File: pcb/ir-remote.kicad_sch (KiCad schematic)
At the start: 109 parts, among them J1 Jack_RCA_Stereo, J12 Conn_01x04, J2 Jack_RCA_Stereo, J3 Conn_02x04, J4 USB-C_Receptacle_Molex_217179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, U1 STM32G431CBTx, U10 LMR62421XMF, U2 TSOP38238, U3 NE5532, U4 NE5532, U5 LP5024RSMR, U6 USBLC6-2SC6, U7 DRV8210DRLR, U9 PCM3060PW, X10 16MHz_18pF_FA238

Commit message: PCB WIP
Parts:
- removed C129, C132, C138: 10uF_0805_25V, 4ms_Capacitor:C_0805, symbol 4ms_Capacitor:10uF_0805_25V
- removed C18: 100nF_0603_16V, 4ms_Capacitor:C_0603, symbol 4ms_Capacitor:100nF_0603_16V
- removed C32: 2.2uF_0603_25V, 4ms_Capacitor:C_0603, symbol 4ms_Capacitor:2.2uF_0603_25V
- removed C6: 1nF_0603_50V, 4ms_Capacitor:C_0603, symbol 4ms_Capacitor:1nF_0603_50V
- removed D1: D_SOD-323F_DNP, 4ms_Diode:D_SOD-123F, symbol 4ms_Diode:D_SOD-323F_DNP
- removed L1: 2.2uH_2.4A_2016, Inductor_SMD:L_Taiyo-Yuden_NR-20xx_HandSoldering, symbol 4ms_Inductor:2.2uH_2.4A_2016
- removed LED1, LED2, LED3, LED4, LED5, LED6, LED7, LED8: RGB_CA_RightAngle, 4ms_LED:LED_Kingbright_APFA2507LQBDSEEZGKC_2.5x1.0mm_Horizontal_RGB, symbol 4ms_LED:RGB_CA_RightAngle
- removed R13, R2, R4: 10k_0603, 4ms_Resistor:R_0603, symbol 4ms_Resistor_0603:10k_0603
- removed R21: 4.99k_0603, 4ms_Resistor:R_0603, symbol 4ms_Resistor_0603:4.99k_0603
- removed R3: 42.2k_0603, 4ms_Resistor:R_0603, symbol 4ms_Resistor_0603:42.2k_0603
- removed U10: LMR62421XMF, Package_TO_SOT_SMD:SOT-23-5, symbol 4ms_IC:LMR62421XMF
- removed U5: LP5024RSMR, 4ms_Package_QFP:QFN-32-1EP_4x4mm_P0.4mm_EP2.65x2.65mm, symbol 4ms_IC:LP5024RSMR
- added C300: 1uF_0402_25V, 4ms_Capacitor:C_0402, symbol 4ms_Capacitor:1uF_0402_25V
- added C303, C6: 10uF_0805_25V, 4ms_Capacitor:C_0805, symbol 4ms_Capacitor:10uF_0805_25V
- added L3: 10uH_0805_0.5A, 4ms_Resistor:R_0805_2012Metric, symbol 4ms_Inductor:10uH_0805_0.5A
- added R4: 71.5k_0603, 4ms_Resistor:R_0603, symbol 4ms_Resistor_0603:71.5k_0603
- added R5: 10k_0603, 4ms_Resistor:R_0603, symbol 4ms_Resistor_0603:10k_0603
- added U112: TLV61046ADB, Package_TO_SOT_SMD:SOT-23-6, symbol Regulator_Switching:TLV61046ADB
- J1, J2: footprint (none) -> 4ms_Jack:RCA_Stereo_SwitchCraft-PJRAS2X1S
- POT1: footprint 4ms_Potentiometer: -> 4ms_Potentiometer:Slider_Dual_Motorized_PSM60-081A-xxx
- U7: JLCPCB ID (none) -> C3681297
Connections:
- net +5VA: now also C100.2, C102.2, D101.2 (cathode), D102.2 (cathode), U3.8 (V+), U4.8 (V+)
- net GND: now also C300.2, C303.2, C6.2, R5.2, U112.2 (GND)
- net I2C_SCL: now also U1.39 (PA15); no longer U1.31 (PA9)
- net I2C_SDA: now also U1.44 (PB7); no longer U1.30 (PA8)
- net MOT+: now also U1.31 (PA9)
- net MOT-: now also U1.30 (PA8)
- net VDD: now also U7.5 (VM), C303.1, C6.1, R4.1, U112.5 (VOUT); no longer C100.2, C102.2, D101.2 (cathode), D102.2 (cathode), U3.8 (V+), U4.8 (V+)
- net V_USB: now also C300.1, L3.1, U112.4 (EN), U112.6 (VI); no longer U7.5 (VM)
- net at POT1.MOTORA: now also U7.6 (OUT1); no longer U7.4 (OUT2)
- net at POT1.MOTORB: now also U7.4 (OUT2); no longer U7.6 (OUT1)
- net USB_DP: now reaches J4.A6 (D+1), J4.B6 (D+2), U6.3 (I/O2), U6.4 (I/O2)
- net USB_DP: now also U1.34 (PA12)
- net USB_DM: now reaches J4.A7 (D-1), J4.B7 (D-2), U6.1 (I/O1), U6.6 (I/O1)
- net USB_DM: now also U1.33 (PA11)
- new net: R4.2, R5.1, U112.3 (FB)
- new net: L3.2, U112.1 (SW)
- no-connect marks 31 -> 25
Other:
- note added: "6.5V Supply"
- note added: "Digital supply"
- note added: "R4/R5 = (VOUt/0.795V - 1)"
- note removed: "LED Driver"
- note removed: "VDD 6.5V"
- moved on the sheet: C31, C4, C40, C49, C5, C51, NT1, NT11, POT1A, POT1B, POT1C, POT1D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

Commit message: PCB WIP
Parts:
- removed C100, C102, C41, C42, C45: 100nF_0402_16V, 4ms_Capacitor:C_0402, symbol 4ms_Capacitor:100nF_0402_16V
- removed C104, C105, C125, C126: 1uF_0402_25V, 4ms_Capacitor:C_0402, symbol 4ms_Capacitor:1uF_0402_25V
- removed C115, C116: 1.5nF_0402_50V, 4ms_Capacitor:C_0402, symbol 4ms_Capacitor:1.5nF_0402_50V
- removed C121, C122, C123, C124: 560pF_0402_50v, 4ms_Capacitor:C_0402, symbol 4ms_Capacitor:560pF_0402_50v
- removed C44: 22uF_0805_25V, 4ms_Capacitor:C_0805, symbol 4ms_Capacitor:22uF_0805_25V
- removed C49: 2.2uF_0603_25V, 4ms_Capacitor:C_0603, symbol 4ms_Capacitor:2.2uF_0603_25V
- removed C51: 10uF_0603_10V, 4ms_Capacitor:C_0603, symbol 4ms_Capacitor:10uF_0603_10V
- removed D101, D102: BAT54S, 4ms_Package_SOT:SOT23-3_PO132, symbol 4ms_Diode:BAT54S
- removed J1, J2: Jack_RCA_Stereo, 4ms_Jack:RCA_Stereo_SwitchCraft-PJRAS2X1S, symbol 4ms_Connector:Jack_RCA_Stereo
- removed NT1: NetTie_2, NetTie:NetTie-2_SMD_Pad0.5mm, symbol Device:NetTie_2
- removed R105, R109, R110, R112, R113, R114, R124, R125: 100k_0402, 4ms_Resistor:R_0402, symbol 4ms_Resistor_0402:100k_0402
- removed R115, R126: 1k_0402, 4ms_Resistor:R_0402, symbol 4ms_Resistor_0402:1k_0402
- removed R119, R120, R121, R122: 10k_0603, 4ms_Resistor:R_0603, symbol 4ms_Resistor_0603:10k_0603
- removed R128, R131, R132, R135: 7.5k_0402, 4ms_Resistor:R_0402, symbol 4ms_Resistor_0402:7.5k_0402
- removed R129, R130, R133, R134: 820Ω_0402, 4ms_Resistor:R_0402, symbol 4ms_Resistor_0402:820Ω_0402
- removed R139, R140: 100Ω_0603, 4ms_Resistor:R_0603, symbol 4ms_Resistor_0603:100Ω_0603
- removed R141, R142: 47k_0603, 4ms_Resistor:R_0603, symbol 4ms_Resistor_0603:47k_0603
- removed R47, R48: 4.7k_0402, 4ms_Resistor:R_0402, symbol 4ms_Resistor_0402:4.7k_0402
- removed U3, U4: NE5532, Package_SO:SOIC-8_5.3x5.3mm_P1.27mm, symbol Amplifier_Operational:NE5532
- removed U9: PCM3060PW, Package_SO:TSSOP-28_4.4x9.7mm_P0.65mm, symbol 4ms_IC:PCM3060PW
- removed V1: AP2120N-5.0TRG1, 4ms_Package_SOT:SOT23-3_PO132, symbol 4ms_Regulator:AP2120N-5.0TRG1
- added C10, C11, C13, C15, C27, C28, C29, C30: 10uF_0603_10V, 4ms_Capacitor:C_0603, symbol 4ms_Capacitor:10uF_0603_10V
- added C12, C14, C33, C9: 0.1uF_0603_16V, 4ms_Capacitor:C_0603, symbol 4ms_Capacitor:0.1uF_0603_16V
- added C16, C19, C20, C21, C26, C32: 1uF_0603_25V, 4ms_Capacitor:C_0603, symbol 4ms_Capacitor:1uF_0603_25V
- added C17, C18: 22uF_1206_25V, 4ms_Capacitor:C_1206, symbol 4ms_Capacitor:22uF_1206_25V
- added C22, C23: 47nF_0603_35V, 4ms_Capacitor:C_0603, symbol 4ms_Capacitor:47nF_0603_35V
- added C7, C8: 47pF_0603_50V, 4ms_Capacitor:C_0603, symbol 4ms_Capacitor:47pF_0603_50V
- added J1, J2, J8: Conn_01x02, 4ms_Connector:Pins_1x02_2.54mm_TH, symbol 4ms_Connector:Conn_01x02
- added J5, J7: Jack_RCA_Stereo, 4ms_Jack:RCA_Stereo_SwitchCraft-PJRAS2X1S, symbol 4ms_Connector:Jack_RCA_Stereo
- added J6: Conn_01x03, 4ms_Connector:Pins_1x03_2.54mm_TH, symbol 4ms_Connector:Conn_01x03
- added JP1: SolderJumper_2_Open, 4ms_SolderJumper:JUMPER_SMD_1x2, symbol 4ms_Net_Tie:SolderJumper_2_Open
- added NT2: NetTie, 4ms_SolderJumper:NetTie-2_SMD_Pad0.16mm_6mil, symbol 4ms_Net_Tie:NetTie
- added R10, R11: 1k_0603, 4ms_Resistor:R_0603, symbol 4ms_Resistor_0603:1k_0603
- added R12, R9: 4.7k_0603, 4ms_Resistor:R_0603, symbol 4ms_Resistor_0603:4.7k_0603
- added R13, R16: 100Ω_0603, 4ms_Resistor:R_0603, symbol 4ms_Resistor_0603:100Ω_0603
- added R14, R15: 100k_0603, 4ms_Resistor:R_0603, symbol 4ms_Resistor_0603:100k_0603
- added R2, R3, R6, R7, R8: 27Ω_0603, 4ms_Resistor:R_0603, symbol 4ms_Resistor_0603:27Ω_0603
- added TP1, TP11, TP12, TP13, TP14, TP2, TP3, TP4, TP5, TP6, TP7, TP8: TestPoint, 4ms_TestPoint:TestPoint_WireHole, symbol 4ms_Connector:TestPoint
- added U3, U4: TLV74018, 4ms_Package_SOT:SOT-23-5, symbol 4ms_Regulator:TLV74018PDBV
- added U5: TLV320AIC3204, Package_DFN_QFN:QFN-32-1EP_5x5mm_P0.5mm_EP3.45x3.45mm_ThermalVias, symbol 4ms_IC:TLV320AIC3204
- added U8: TAR5S33U, 4ms_Package_SOT:SOT-563-5, symbol 4ms_Regulator:TAR5S33U
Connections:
- net +3V3: now also C11.1, C33.1, R9.1, U5.6 (IOVDD)
- net CODEC_RESET: now also U1.45 (PB8), U5.31 (RESET_N)
- net GND: now also C10.2, C11.2, C14.1, C27.2, C28.2, C29.2, C30.2, C32.2, C33.2, J8.1 (Pin_1), JP1.1 (A), NT2.1, R12.1, U3.2 (GND), U4.2 (GND), U5.28 (DVSS), U5.33 (PAD), U5.7 (IOVSS), U8.2 (GND); no longer U7.9 (GND)
- net GNDA: now also C12.1, C13.2, C15.2, C16.2, C22.2, C23.2, C7.2, C8.2, C9.1, J5.S1, J5.S2, J6.2 (Pin_2), J7.S1, J7.S2, NT2.2, R14.2, R15.2, U5.17 (AVSS)
- net I2C_SCL: now also U5.9 (SCL_SS_N)
- net I2C_SDA: now also U5.10 (SDA_MOSI)
- net SAI_FS: now also R8.1
- net SAI_MCLK: now also R6.1
- net SAI_SCK: now also R7.1
- net SAI_SD_A: now also R2.1
- net SAI_SD_B: now also R3.1
- net V_USB: now also C40.1, V12.1 (VI), C28.1, C29.1, C32.1, U3.1 (IN), U3.3 (EN), U4.1 (IN), U4.3 (EN), U8.1 (EN), U8.5 (IN)
- net at J4.SH1 (Shield1), J4.SH2 (Shield2), J4.SH3 (Shield3)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: now also J8.2 (Pin_2)
- net VDD renamed Vmotor
- net Vmotor: no longer C40.1, V12.1 (VI)
- new net: R7.2, U5.2 (BCLK)
- new net: C14.2, U8.3 (Noise)
- new net: C19.1, R10.2
- new net: R8.2, U5.3 (WCLK)
- new net: C13.1, J1.1 (Pin_1), U5.24 (AVDD)
- new net: C19.2, J5.T2, R14.1
- new net: C23.1, J7.T2, R16.2
- new net: JP1.2 (B), R9.2, U5.30 (LDO_SELECT)
- new net: C20.1, R11.2
- new net: C21.2, R13.1
- new net: C22.1, J7.T1, R13.2
- new net: C18.1, U5.27 (HPR)
- new net: C18.2, J6.3 (Pin_3)
- new net: C26.2, R16.1
- new net: C20.2, J5.T1, R15.1
- new net: R6.2, U5.1 (MCLK)
- new net: C10.1, J2.1 (Pin_1), U5.29 (DVDD)
- new net: C17.1, U5.25 (HPL)
- new net: C17.2, J6.1 (Pin_1)
- new net: R12.2, U5.12 (SPI_SELECT)
- new net: R3.2, U5.5 (DOUT_MFP2)
- new net: C9.2, U5.18 (REF)
- new net: R2.2, U5.4 (DIN_MFP1)
- new net AVDD: C27.1, J2.2 (Pin_2), U3.5 (OUT)
- new net DVDD: C30.1, J1.2 (Pin_2), U4.5 (OUT)
- new net GPIO: TP11.1, U5.32 (GPIO_MFP5)
- new net IN2_L: TP5.1, U5.15 (IN2_L)
- new net IN2_R: TP6.1, U5.16 (IN2_R)
- new net IN3_L: TP7.1, U5.20 (IN3_L)
- new net IN3_R: TP8.1, U5.21 (IN3_R)
- new net INL: C7.1, R10.1, TP3.1, U5.13 (IN1_L)
- new net INR: C8.1, R11.1, TP4.1, U5.14 (IN1_R)
- new net LINEOUT_L: C21.1, TP1.1, U5.22 (LOL)
- new net LINEOUT_R: C26.1, TP2.1, U5.23 (LOR)
- new net MICBIAS: TP14.1, U5.19 (MICBIAS)
- new net MISO: TP13.1, U5.11 (MISO_MFP4)
- new net SCK_MICDET: TP12.1, U5.8 (SCLK_MFP3)
- new net VLDO: C12.2, C15.1, C16.1, U5.26 (LDOIN_HPVDD), U8.4 (OUT)
- no-connect marks 25 -> 24
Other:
- note added: "6.5V Motor Supply"
- note added: "ADC Ref."
- note added: "Avdd 1.8V or int.LDO"
- note added: "Codec Supply"
- note added: "Dvdd: 1.8V or int.LDO"
- note added: "H=EnableLDO"
- note added: "H=SPI,L=I2C"
- note added: "USB5V => LDO IN (->HP, AVDD, DVDD)"
- note removed: "6.5V Supply"
- note removed: "AUDIO INS"
- note removed: "AUDIO OUTS"
- note removed: "CODEC"
- note removed: "CODEC POWER"
- moved on the sheet: C300, C303, C35, C36, C37, C38, C39, C6, J4, L11, L3, POT1C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

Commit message: PCB WIP
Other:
- moved on the sheet: C10, C13, J1, J2

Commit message: PCB routed and ready for review
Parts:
- removed J3: Conn_02x04, 4ms_Connector:Pins_2x04_2.54mm_TH, symbol 4ms_Connector:Conn_02x04
- added C34: 100nF_0603_16V, 4ms_Capacitor:C_0603, symbol 4ms_Capacitor:100nF_0603_16V
- added J3: Pins_02x04_P2.54mm_SMT, 4ms_Connector:Pins_2x04_P2.54mm_Vertical_SMD, symbol 4ms_Connector:Pins_02x04_P2.54mm_SMT
- U3, U4: JLCPCB ID (none) -> C3746861; Part Number TLV74018PDBV -> TLV74018PDBVR
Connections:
- net +3V3REF: now also C31.2, POT1.1 (Left); no longer POT1.3 (Right)
- net ADCGND: now also POT1.3 (Right), C34.1; no longer C31.2, POT1.1 (Left)
- net AVDD: now also C30.1, J1.2 (Pin_2), U4.5 (OUT); no longer C27.1, J2.2 (Pin_2), U3.5 (OUT)
- net DEBUG2: now also J3.5 (Pin_5)
- net DEBUG3: now also J3.7 (Pin_7)
- net DVDD: now also C27.1, J2.2 (Pin_2), U3.5 (OUT); no longer C30.1, J1.2 (Pin_2), U4.5 (OUT)
- net GND: now also J3.2 (Pin_2), J3.4 (Pin_4), J3.6 (Pin_6), J3.8 (Pin_8)
- net IN2_R: now also TP14.1; no longer TP6.1
- net IN3_R: now also TP6.1; no longer TP8.1
- net LINEOUT_L: now also C26.1, TP2.1; no longer C21.1, TP1.1
- net LINEOUT_R: now also C21.1, TP1.1; no longer C26.1, TP2.1
- net MICBIAS: now also TP8.1; no longer TP14.1
- net Slider_ADC: now also C34.2
- net UART_RX: now also J3.3 (Pin_3)
- net UART_TX: now also J3.1 (Pin_1)
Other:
- moved on the sheet: C2, C21, C22, C23, C26, C31, C35, C36, C37, C38, C39, C4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

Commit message: Adjust PCB edges and mounting holes to fit enclosure
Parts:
- added H1, H2, H3, H4: MountingHole, 4ms_Hardware:MountingHole_Screw_3mmHole_5.3mmHead, symbol Mechanical:MountingHole

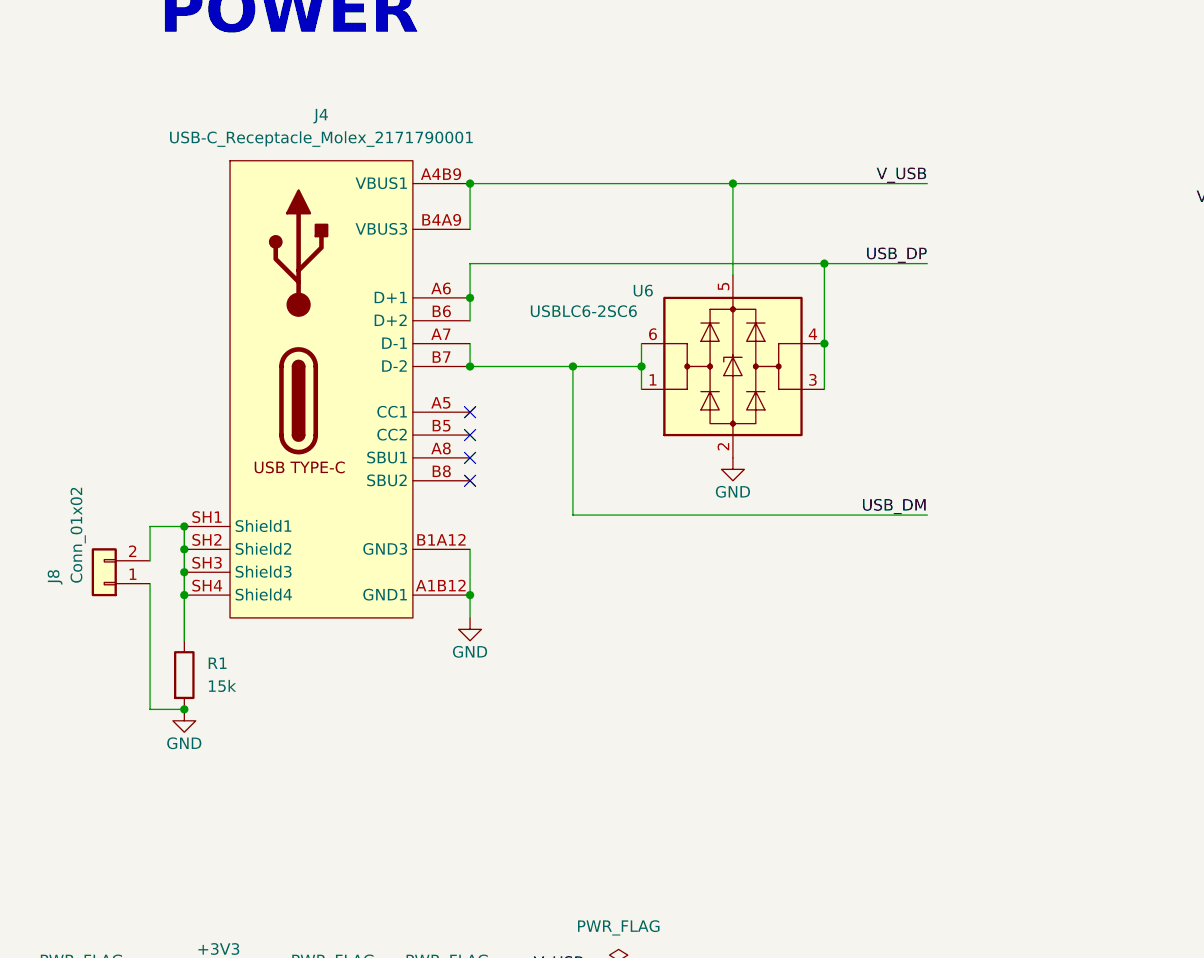
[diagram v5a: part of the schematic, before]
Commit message: PCB: add missing 5.1k USB pull-downs
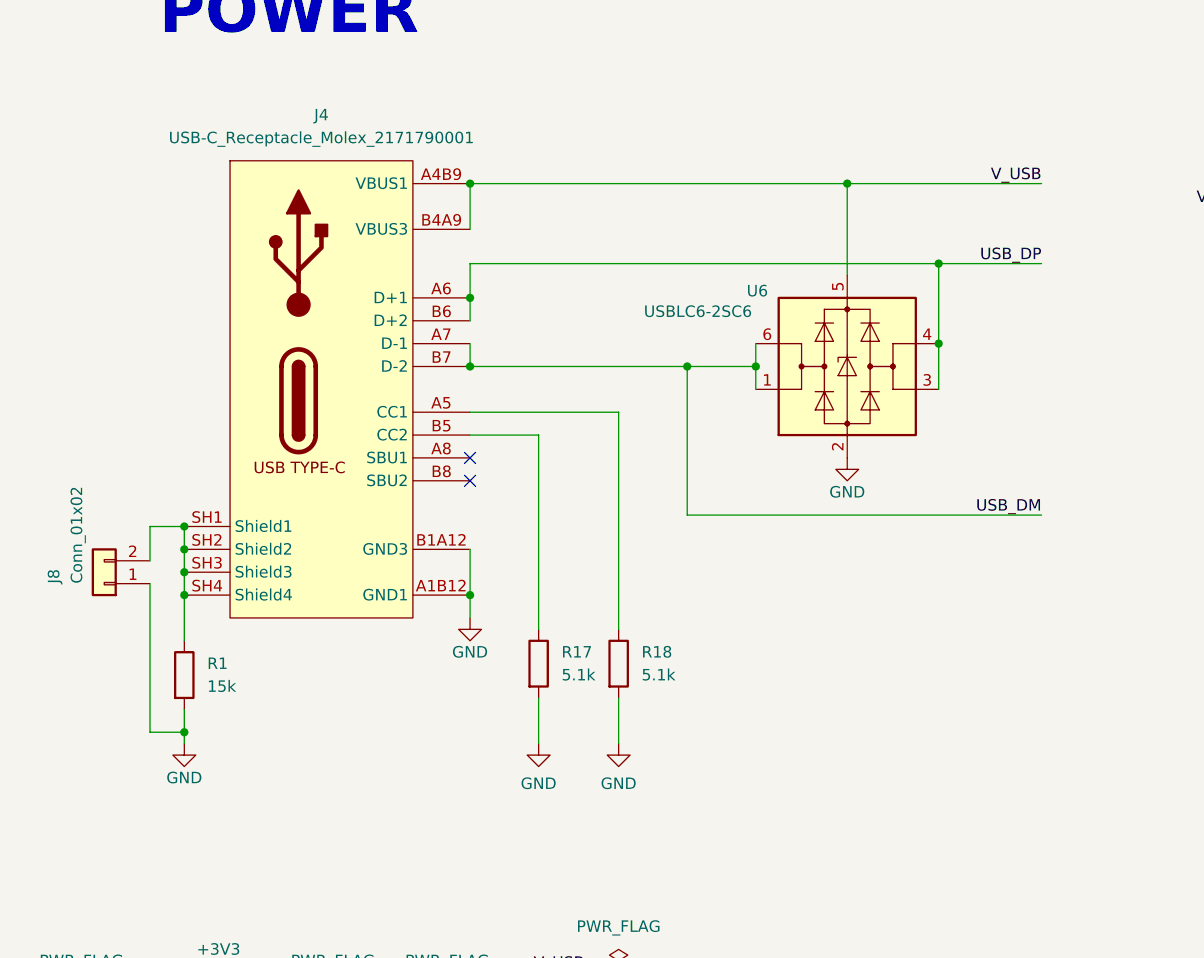
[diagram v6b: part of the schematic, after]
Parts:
- added R17, R18: 5.1k_0603, 4ms_Resistor:R_0603, symbol 4ms_Resistor_0603:5.1k_0603
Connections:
- net GND: now also R17.2, R18.2
- net at J4.A5 (CC1): now also R18.1
- net at J4.B5 (CC2): now also R17.1
- no-connect marks 24 -> 22
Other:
- moved on the sheet: U6

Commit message: pcb: 20R=>33R, 2.2uF=>10uF. Change some JLC # to cheaper parts
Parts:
- C40: value 2.2uF_0603_25V -> 10uF_0603_10V; symbol 4ms_Capacitor:2.2uF_0603_25V -> 4ms_Capacitor:10uF_0603_10V; Display 2.2uF -> 10uF/10V; JLCPCB ID C57895 -> C19702; Part Number GRM188R6YA225KA12D -> GRM188R61A106KE69D; Specifications 2.2uF, Min 25V 10% X5R -> 10uF, Min. 10V X5R 10%
- R2, R3, R6, R7, R8: value 27Ω_0603 -> 33Ω_0603; symbol 4ms_Resistor_0603:27Ω_0603 -> 4ms_Resistor_0603:33Ω_0603; Display 27Ω -> 33Ω; JLCPCB ID C137753 -> C23140; Part Number RC0603FR-0727RL -> RC0603FR-0733RL; Specifications 27Ω, 1%, 1/10W, 0603 -> 33Ω, 1%, 1/10W, 0603
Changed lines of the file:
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@@
 	)
 	(symbol
-		(lib_id "4ms_Resistor_0603:27Ω_0603")
+		(lib_id "4ms_Resistor_0603:33Ω_0603")
 		(at 50.8 229.87 90)
 		(unit 1)
@@
 			)
 		)
-		(property "Value" "27Ω_0603"
+		(property "Value" "33Ω_0603"
 			(at 50.8 232.41 90)
 			(effects
@@
 			)
 		)
-		(property "Description" "27Ω, 1%, 1/10W, 0603"
+		(property "Description" "33Ω, 1%, 1/10W, 0603"
 			(at 50.8 229.87 0)
 			(effects
@@
 			)
 		)
-		(property "Specifications" "27Ω, 1%, 1/10W, 0603"
+		(property "Specifications" "33Ω, 1%, 1/10W, 0603"
 			(at 58.42 232.41 0)
 			(effects
@@
 			)
 		)
-		(property "Part Number" "RC0603FR-0727RL"
+		(property "Part Number" "RC0603FR-0733RL"
 			(at 61.976 232.41 0)
 			(effects
@@
 			)
 		)
-		(property "Display" "27Ω"
-			(at 50.546 229.87 90)
+		(property "Display" "33Ω"
+			(at 51.054 229.87 90)
 			(effects
 				(font
@@
 			)
 		)
-		(property "JLCPCB ID" "C137753"
+		(property "JLCPCB ID" "C23140"
 			(at 65.532 232.41 0)
 			(effects
@@
 	)
 	(symbol
-		(lib_id "4ms_Resistor_0603:27Ω_0603")
+		(lib_id "4ms_Resistor_0603:33Ω_0603")
 		(at 50.8 227.33 90)
 		(unit 1)
@@
 			)
 		)
-		(property "Value" "27Ω_0603"
+		(property "Value" "33Ω_0603"
 			(at 50.8 229.87 90)
 			(effects
@@
 			)
 		)
-		(property "Description" "27Ω, 1%, 1/10W, 0603"
+		(property "Description" "33Ω, 1%, 1/10W, 0603"
 			(at 50.8 227.33 0)
 			(effects
@@
 			)
 		)
-		(property "Specifications" "27Ω, 1%, 1/10W, 0603"
+		(property "Specifications" "33Ω, 1%, 1/10W, 0603"
 			(at 58.42 229.87 0)
 			(effects
@@
 			)
 		)
-		(property "Part Number" "RC0603FR-0727RL"
+		(property "Part Number" "RC0603FR-0733RL"
 			(at 61.976 229.87 0)
 			(effects
@@
 			)
 		)
-		(property "Display" "27Ω"
-			(at 50.546 227.33 90)
+		(property "Display" "33Ω"
+			(at 51.054 227.33 90)
 			(effects
 				(font
@@
 			)
 		)
-		(property "JLCPCB ID" "C137753"
+		(property "JLCPCB ID" "C23140"
 			(at 65.532 229.87 0)
 			(effects
@@
 	)
 	(symbol
-		(lib_id "4ms_Capacitor:2.2uF_0603_25V")
+		(lib_id "4ms_Capacitor:10uF_0603_10V")
 		(at 321.31 45.72 0)
 		(unit 1)
@@
 		(fields_autoplaced yes)
 		(property "Reference" "C40"
-			(at 323.85 45.0913 0)
+			(at 323.85 44.4562 0)
 			(effects
 				(font
@@
 			)
 		)
-		(property "Value" "2.2uF_0603_25V"
+		(property "Value" "10uF_0603_10V"
 			(at 321.31 41.91 0)
 			(effects
@@
 		)
 		(property "Footprint" "4ms_Capacitor:C_0603"
-			(at 329.565 58.42 0)
+			(at 318.77 50.8 0)
 			(effects
 				(font
 					(size 1.27 1.27)
 				)
+				(justify left)
 				(hide yes)
 			)
@@
 			)
 		)
-		(property "Description" ""
+		(property "Description" "10uF, Min. 10V X5R 10%"
 			(at 321.31 45.72 0)
 			(effects
@@
 					(size 1.27 1.27)
 				)
+				(hide yes)
 			)
 		)
-		(property "Specifications" "2.2uF, Min 25V 10% X5R"
+		(property "Specifications" "10uF, Min. 10V X5R 10%"
 			(at 318.77 53.594 0)
 			(effects
@@
 			)
 		)
-		(property "Part Number" "GRM188R6YA225KA12D"
+		(property "Part Number" "GRM188R61A106KE69D"
 			(at 318.77 56.642 0)
 			(effects
@@
 			)
 		)
-		(property "Display" "2.2uF"
-			(at 323.85 47.6313 0)
+		(property "Display" "10uF/10V"
+			(at 323.85 46.9962 0)
 			(effects
 				(font
@@
 			)
 		)
-		(property "JLCPCB ID" "C57895"
-			(at 321.31 45.72 0)
+		(property "JLCPCB ID" "C19702"
+			(at 322.58 58.42 0)
 			(effects
 				(font
@@
 	)
 	(symbol
-		(lib_id "4ms_Resistor_0603:27Ω_0603")
+		(lib_id "4ms_Resistor_0603:33Ω_0603")
 		(at 50.8 232.41 90)
 		(unit 1)
@@
 			)
 		)
-		(property "Value" "27Ω_0603"
+		(property "Value" "33Ω_0603"
 			(at 50.8 234.95 90)
 			(effects
@@
 			)
 		)
-		(property "Description" "27Ω, 1%, 1/10W, 0603"
+		(property "Description" "33Ω, 1%, 1/10W, 0603"
 			(at 50.8 232.41 0)
 			(effects
@@
 			)
 		)
-		(property "Specifications" "27Ω, 1%, 1/10W, 0603"
+		(property "Specifications" "33Ω, 1%, 1/10W, 0603"
 			(at 58.42 234.95 0)
 			(effects
@@
 			)
 		)
-		(property "Part Number" "RC0603FR-0727RL"
+		(property "Part Number" "RC0603FR-0733RL"
 			(at 61.976 234.95 0)
 			(effects
@@
 			)
 		)
-		(property "Display" "27Ω"
-			(at 50.546 232.41 90)
+		(property "Display" "33Ω"
+			(at 51.054 232.41 90)
 			(effects
 				(font
@@
 			)
 		)
-		(property "JLCPCB ID" "C137753"
+		(property "JLCPCB ID" "C23140"
 			(at 65.532 234.95 0)
 			(effects
@@
 	)
 	(symbol
-		(lib_id "4ms_Resistor_0603:27Ω_0603")
+		(lib_id "4ms_Resistor_0603:33Ω_0603")
 		(at 50.8 234.95 90)
 		(unit 1)
@@
 			)
 		)
-		(property "Value" "27Ω_0603"
+		(property "Value" "33Ω_0603"
 			(at 50.8 237.49 90)
 			(effects
@@
 			)
 		)
-		(property "Description" "27Ω, 1%, 1/10W, 0603"
+		(property "Description" "33Ω, 1%, 1/10W, 0603"
 			(at 50.8 234.95 0)
 			(effects
@@
 			)
 		)
-		(property "Specifications" "27Ω, 1%, 1/10W, 0603"
+		(property "Specifications" "33Ω, 1%, 1/10W, 0603"
 			(at 58.42 237.49 0)
 			(effects
@@
 			)
 		)
-		(property "Part Number" "RC0603FR-0727RL"
+		(property "Part Number" "RC0603FR-0733RL"
 			(at 61.976 237.49 0)
 			(effects
@@
 			)
 		)
-		(property "Display" "27Ω"
-			(at 50.546 234.95 90)
+		(property "Display" "33Ω"
+			(at 51.054 234.95 90)
 			(effects
 				(font
@@
 			)
 		)
-		(property "JLCPCB ID" "C137753"
+		(property "JLCPCB ID" "C23140"
 			(at 65.532 237.49 0)
 			(effects
@@
 	)
 	(symbol
-		(lib_id "4ms_Resistor_0603:27Ω_0603")
+		(lib_id "4ms_Resistor_0603:33Ω_0603")
 		(at 50.8 237.49 90)
 		(unit 1)
@@
 			)
 		)
-		(property "Value" "27Ω_0603"
+		(property "Value" "33Ω_0603"
 			(at 50.8 240.03 90)
 			(effects
@@
 			)
 		)
-		(property "Description" "27Ω, 1%, 1/10W, 0603"
+		(property "Description" "33Ω, 1%, 1/10W, 0603"
 			(at 50.8 237.49 0)
 			(effects
@@
 			)
 		)
-		(property "Specifications" "27Ω, 1%, 1/10W, 0603"
+		(property "Specifications" "33Ω, 1%, 1/10W, 0603"
 			(at 58.42 240.03 0)
 			(effects
@@
 			)
 		)
-		(property "Part Number" "RC0603FR-0727RL"
+		(property "Part Number" "RC0603FR-0733RL"
 			(at 61.976 240.03 0)
 			(effects
@@
 			)
 		)
-		(property "Display" "27Ω"
-			(at 50.546 237.49 90)
+		(property "Display" "33Ω"
+			(at 51.054 237.49 90)
 			(effects
 				(font
@@
 			)
 		)
-		(property "JLCPCB ID" "C137753"
+		(property "JLCPCB ID" "C23140"
 			(at 65.532 240.03 0)
 			(effects
